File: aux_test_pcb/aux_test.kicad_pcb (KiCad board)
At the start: 2 copper layers, 35.6 x 35.6 mm, 15 parts, among them J1 AUX_TEST, J2 SOL, J3 PUMP, J4 SERVO

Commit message: aux_test minor mods
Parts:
- D1: value LEL_SOL -> SOL
- D2: value LED_Vin -> Vin
- D3: value LED_PUMP -> PUMP
- D4: value LED_SVCC -> SVCC
- R1, R2: value 150E -> 390E
- R3, R4: value 150E -> 330E
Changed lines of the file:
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@@
     (links 21)
     (no_connects 0)
-    (area 55.169999 29.134999 90.880001 64.845001)
+    (area 43.914288 28.997 90.880001 72.55)
     (thickness 1.6)
     (drawings 14)
-    (tracks 73)
+    (tracks 72)
     (zones 0)
     (modules 15)
@@
     (visible_elements FFFFFF7F)
     (pcbplotparams
-      (layerselection 0x00030_80000001)
+      (layerselection 0x00130_80000001)
       (usegerberextensions false)
-      (excludeedgelayer true)
+      (excludeedgelayer false)
       (linewidth 0.050800)
-      (plotframeref false)
+      (plotframeref true)
       (viasonmask false)
       (mode 1)
@@
       (plotvalue true)
       (plotinvisibletext false)
-      (padsonsilk false)
+      (padsonsilk true)
       (subtractmaskfromsilk false)
-      (outputformat 1)
+      (outputformat 4)
       (mirror false)
-      (drillshape 1)
+      (drillshape 2)
       (scaleselection 1)
-      (outputdirectory ""))
+      (outputdirectory aux_test_pdf/))
   )
   (net 0 "")
@@
       (effects (font (size 1 1) (thickness 0.15)))
     )
-    (fp_text value SERVO (at -3.81 2.54 90) (layer F.SilkS)
+    (fp_text value SERVO (at 5.08 1.27 90) (layer F.SilkS)
       (effects (font (size 1 1) (thickness 0.15)))
     )
@@
     (fp_line (start 1.8 6.85) (end 1.8 -1.8) (layer F.CrtYd) (width 0.05))
     (fp_line (start 1.8 -1.8) (end -1.8 -1.8) (layer F.CrtYd) (width 0.05))
-    (fp_text user %R (at -5.715 2.54 90) (layer F.SilkS)
+    (fp_text user %R (at 2.54 7.62 90) (layer F.SilkS)
       (effects (font (size 1 1) (thickness 0.15)))
     )
@@
       (effects (font (size 1 1) (thickness 0.15)))
     )
-    (fp_text value LEL_SOL (at 0 -3.81 90) (layer F.SilkS)
+    (fp_text value SOL (at 0 -3.81 90) (layer F.SilkS)
       (effects (font (size 1 1) (thickness 0.15)))
     )
@@
       (effects (font (size 1 1) (thickness 0.15)))
     )
-    (fp_text value LED_Vin (at 0 3.81 270) (layer F.SilkS)
+    (fp_text value Vin (at 0 3.81 270) (layer F.SilkS)
       (effects (font (size 1 1) (thickness 0.15)))
     )
@@
       (effects (font (size 1 1) (thickness 0.15)))
     )
-    (fp_text value LED_PUMP (at 0 3.81 270) (layer F.SilkS)
+    (fp_text value PUMP (at 0 3.81 270) (layer F.SilkS)
       (effects (font (size 1 1) (thickness 0.15)))
     )
@@
       (effects (font (size 1 1) (thickness 0.15)))
     )
-    (fp_text value LED_SVCC (at 0 -3.81 90) (layer F.SilkS)
+    (fp_text value SVCC (at 0 -3.81 90) (layer F.SilkS)
       (effects (font (size 1 1) (thickness 0.15)))
     )
@@
       (effects (font (size 1 1) (thickness 0.15)))
     )
-    (fp_text value 150E (at 0 -0.508) (layer F.SilkS) hide
+    (fp_text value 390E (at 0 -0.508) (layer F.SilkS) hide
       (effects (font (size 1 1) (thickness 0.15)))
     )
@@
       (effects (font (size 1 1) (thickness 0.15)))
     )
-    (fp_text value 150E (at 0 -0.508) (layer F.SilkS) hide
+    (fp_text value 390E (at 0 -0.508) (layer F.SilkS) hide
       (effects (font (size 1 1) (thickness 0.15)))
     )
@@
       (effects (font (size 1 1) (thickness 0.15)))
     )
-    (fp_text value 150E (at 0 -0.508) (layer F.SilkS) hide
+    (fp_text value 330E (at 0 -0.508) (layer F.SilkS) hide
       (effects (font (size 1 1) (thickness 0.15)))
     )
@@
       (effects (font (size 1 1) (thickness 0.15)))
     )
-    (fp_text value 150E (at 0 -0.508 180) (layer F.SilkS) hide
+    (fp_text value 330E (at 0 -0.508 180) (layer F.SilkS) hide
       (effects (font (size 1 1) (thickness 0.15)))
     )
@@
   (segment (start 76.835 45.72) (end 80.645 41.91) (width 0.25) (layer F.Cu) (net 9))
   (segment (start 80.645 41.91) (end 84.455 41.91) (width 0.25) (layer F.Cu) (net 9))
+  (segment (start 80.645 59.69) (end 82.55 59.69) (width 1.27) (layer F.Cu) (net 10))
+  (segment (start 82.55 59.69) (end 85.09 57.15) (width 1.27) (layer F.Cu) (net 10))
+  (segment (start 83.82 31.75) (end 76.2 31.75) (width 1.27) (layer F.Cu) (net 10))
+  (segment (start 85.09 57.15) (end 86.995 57.15) (width 1.27) (layer F.Cu) (net 10))
+  (segment (start 86.995 57.15) (end 88.9 55.245) (width 1.27) (layer F.Cu) (net 10))
+  (segment (start 88.9 55.245) (end 88.9 36.83) (width 1.27) (layer F.Cu) (net 10))
+  (segment (start 88.9 36.83) (end 83.82 31.75) (width 1.27) (layer F.Cu) (net 10))
   (segment (start 61.595 49.53) (end 61.595 56.515) (width 1.27) (layer B.Cu) (net 10))
   (segment (start 61.595 56.515) (end 66.04 60.96) (width 1.27) (layer B.Cu) (net 10))
-  (segment (start 88.9 36.83) (end 83.82 31.75) (width 1.27) (layer F.Cu) (net 10))
-  (segment (start 76.2 31.75) (end 83.82 31.75) (width 1.27) (layer F.Cu) (net 10))
-  (segment (start 88.9 55.245) (end 88.9 36.83) (width 1.27) (layer F.Cu) (net 10))
-  (segment (start 86.995 57.15) (end 88.9 55.245) (width 1.27) (layer F.Cu) (net 10))
-  (segment (start 84.455 57.15) (end 86.995 57.15) (width 1.27) (layer F.Cu) (net 10))
-  (segment (start 82.764999 58.840001) (end 84.455 57.15) (width 1.27) (layer F.Cu) (net 10))
-  (segment (start 80.645 59.69) (end 81.494999 58.840001) (width 1.27) (layer F.Cu) (net 10))
-  (segment (start 81.494999 58.840001) (end 82.764999 58.840001) (width 1.27) (layer F.Cu) (net 10))
   (segment (start 80.645 59.69) (end 78.105 62.23) (width 1.27) (layer F.Cu) (net 10))
   (segment (start 69.215 60.96) (end 66.04 60.96) (width 1.27) (layer F.Cu) (net 10))

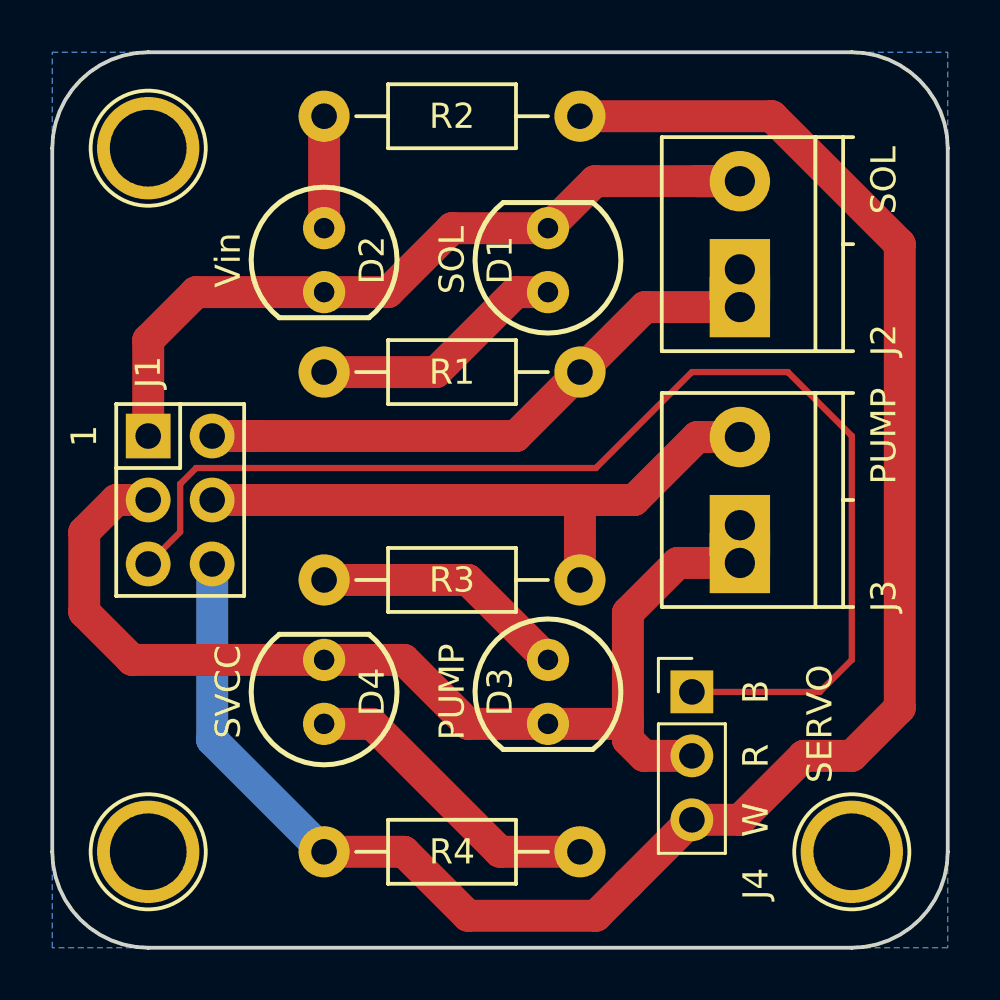
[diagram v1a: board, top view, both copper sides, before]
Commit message: fixed errors in aux_test layout
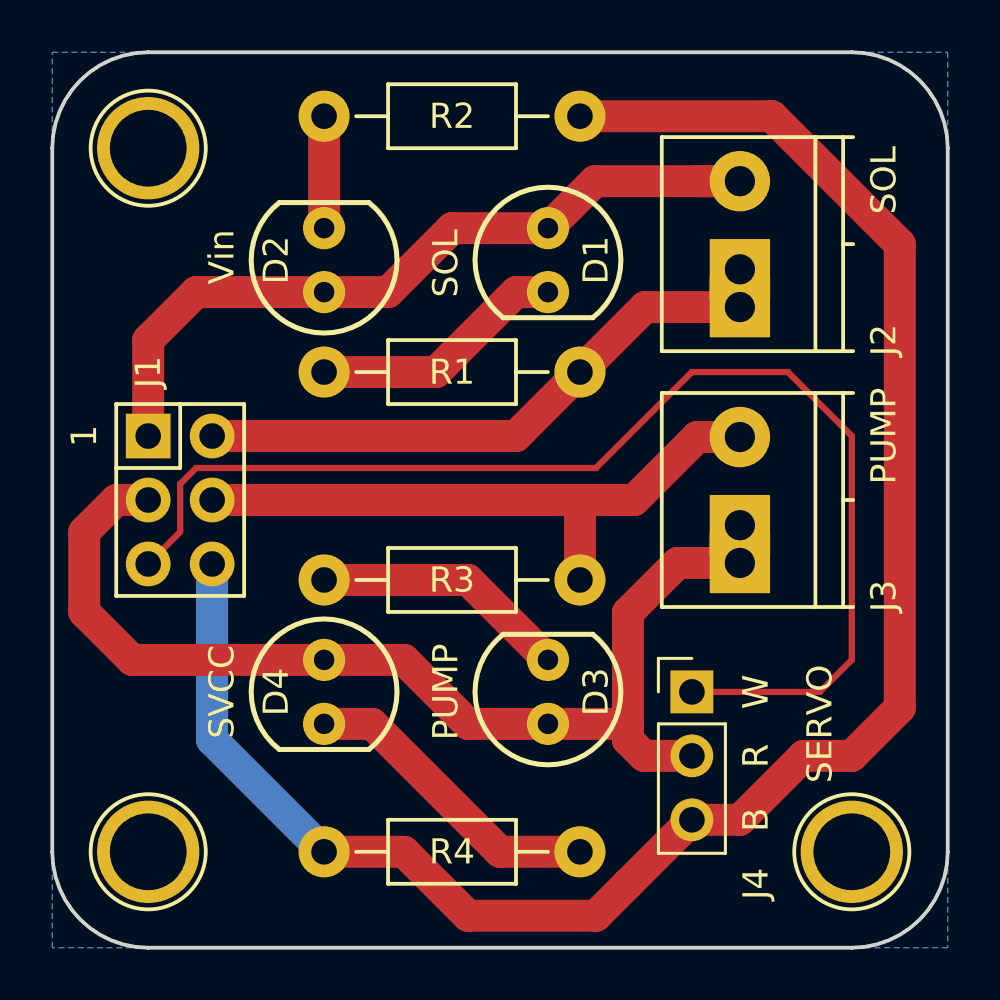
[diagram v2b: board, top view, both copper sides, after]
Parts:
- turned D1 to 270 degrees
- turned D2 to 90 degrees
- turned D3 to 90 degrees
- turned D4 to 270 degrees
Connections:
- D1 pad 1: Net-(D1-Pad1) -> /Vin
- D1 pad 2: /Vin -> Net-(D1-Pad2)
- D2 pad 1: Net-(D2-Pad1) -> /Vin
- D2 pad 2: /Vin -> Net-(D2-Pad2)
- D3 pad 1: Net-(D3-Pad1) -> /SVCC
- D3 pad 2: /SVCC -> Net-(D3-Pad2)
- D4 pad 1: Net-(D4-Pad1) -> /SVCC
- D4 pad 2: /SVCC -> Net-(D4-Pad2)
- R1 pad 1: Net-(D1-Pad1) -> Net-(D1-Pad2)
- R2 pad 1: Net-(D2-Pad1) -> Net-(D2-Pad2)
- R3 pad 1: Net-(D3-Pad1) -> Net-(D3-Pad2)
- R4 pad 1: Net-(D4-Pad1) -> Net-(D4-Pad2)
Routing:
- net Net-(D4-Pad2): track 0.00 -> 12.3 mm
- net Net-(D4-Pad1): track 12.3 -> 0.00 mm
- net Net-(D3-Pad2): track 0.00 -> 10.2 mm
- net Net-(D3-Pad1): track 10.2 -> 0.00 mm
- net Net-(D1-Pad2): track 0.00 -> 10.2 mm
- net Net-(D1-Pad1): track 10.2 -> 0.00 mm
- net Net-(D2-Pad2): track 0.00 -> 4.45 mm
- net Net-(D2-Pad1): track 4.45 -> 0.00 mm

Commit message: updated aux_test PCB
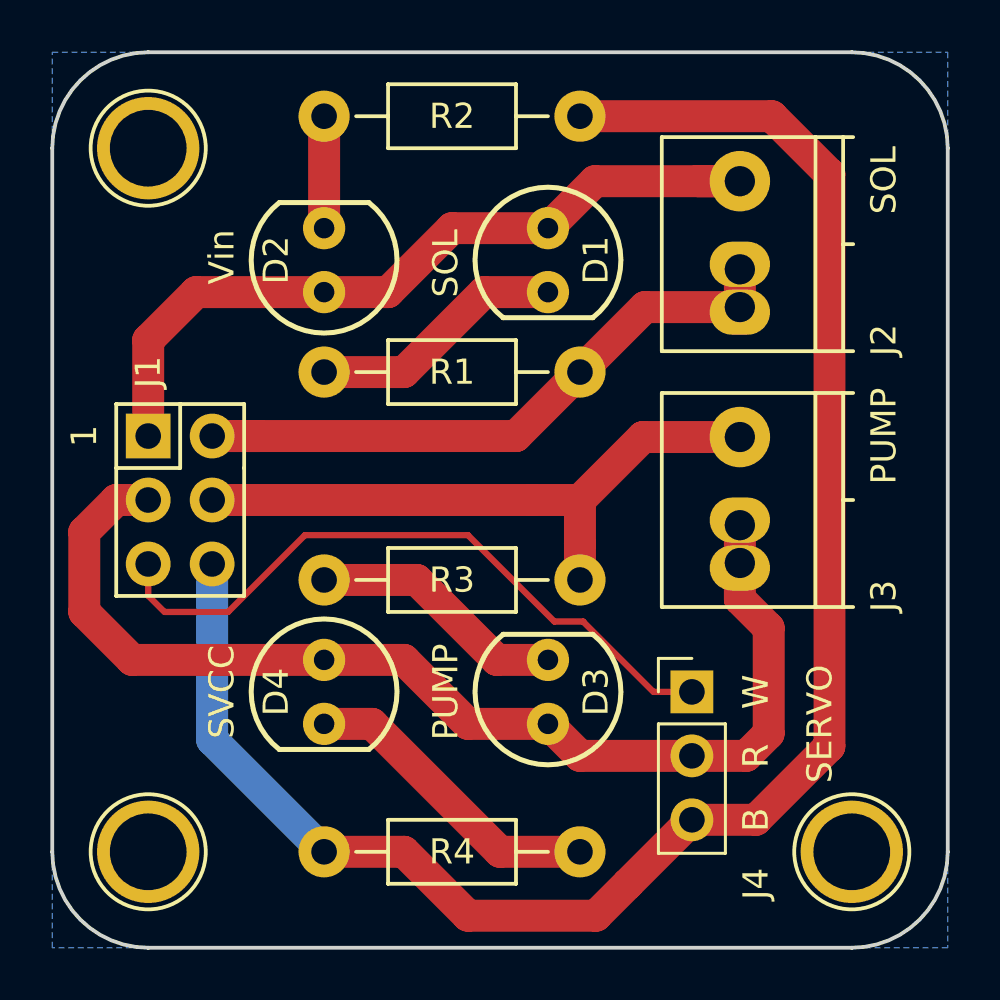
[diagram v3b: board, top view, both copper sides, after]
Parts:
- R1, R2: value 390E -> 470E
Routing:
- net /3(**): track 49.0 -> 27.0 mm
- net /GND: track 73.8 -> 70.8 mm
- net /SVCC: track 44.3 -> 44.9 mm
